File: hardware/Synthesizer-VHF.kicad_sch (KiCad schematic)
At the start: 119 parts, among them J1 Screw_Terminal_01x02, J10 REF_OUT, J11 Header 1x3, J2 Scope, J4 USB-C 2.0 16P, J5 REF_IN, J6 Scope, J7 RFOUTA, J8 Header 1x3, J9 RFOUTB, U1 LM7805A, U11 SN74LVC1GU04DBVR, U2 FT231XQ, U3 ATtiny1616-M, U4 ADF4351, U5 USBLC6-2SC6, U6 LP5907MFX-3.3, U7 ADP150AUJZ-3.3-R7, U8 LP5907MFX-3.3, U9 LP5907MFX-3.3, X1 HCI 8122S-25NQ33FTL

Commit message: diecast-2x2: user layout edits (KiCad save)
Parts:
- removed C44, C45, C46, C47, C48, C49: 100p, Synthesizer:Cap_0402, symbol Device:C
- removed FB2, FB4, FB6: FerriteBead_Small, Inductor_SMD:L_0805_2012Metric, symbol Device:FerriteBead_Small
- removed U7: ADP150AUJZ-3.3-R7, Package_TO_SOT_SMD:SOT-23-5, symbol Synthesizer:ADP150AUJZ-3.3-R7
- added U10: LP5907MFX-3.3, Package_TO_SOT_SMD:SOT-23-5, symbol Regulator_Linear:LP5907MFX-3.3
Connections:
- net 5V: now also U10.1 (IN), U10.3 (EN)
- net GND: now also U10.2 (GND)
- net VCC_1: no longer C13.1, C19.2, C21.2, C27.1, C30.1, U4.28 (DVDD), U4.32 (SDVDD)
- net VDD: no longer C24.1, C25.1, U4.10 (AVDD), U4.6 (Vp)
- net VRF: now also C14.1, U8.5 (OUT)
- net VVCO: now also C39.1, U6.5 (OUT)
- net VADD: now reaches C53.1, U9.5 (OUT)
- net VADD: now also C24.1, C25.1, U4.10 (AVDD), U4.6 (Vp)
- net at D8.2 (A): no longer U3.2 (PA3)
- net REFIN_SEL: no longer names the net of C3.2, R32.2
- new net VDIG: C13.1, C19.2, C21.2, C27.1, C30.1, U10.5 (OUT), U4.28 (DVDD), U4.32 (SDVDD)
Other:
- moved on the sheet: C1, C10, C12, C13, C14, C15, C16, C17, C18, C19, C20, C21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

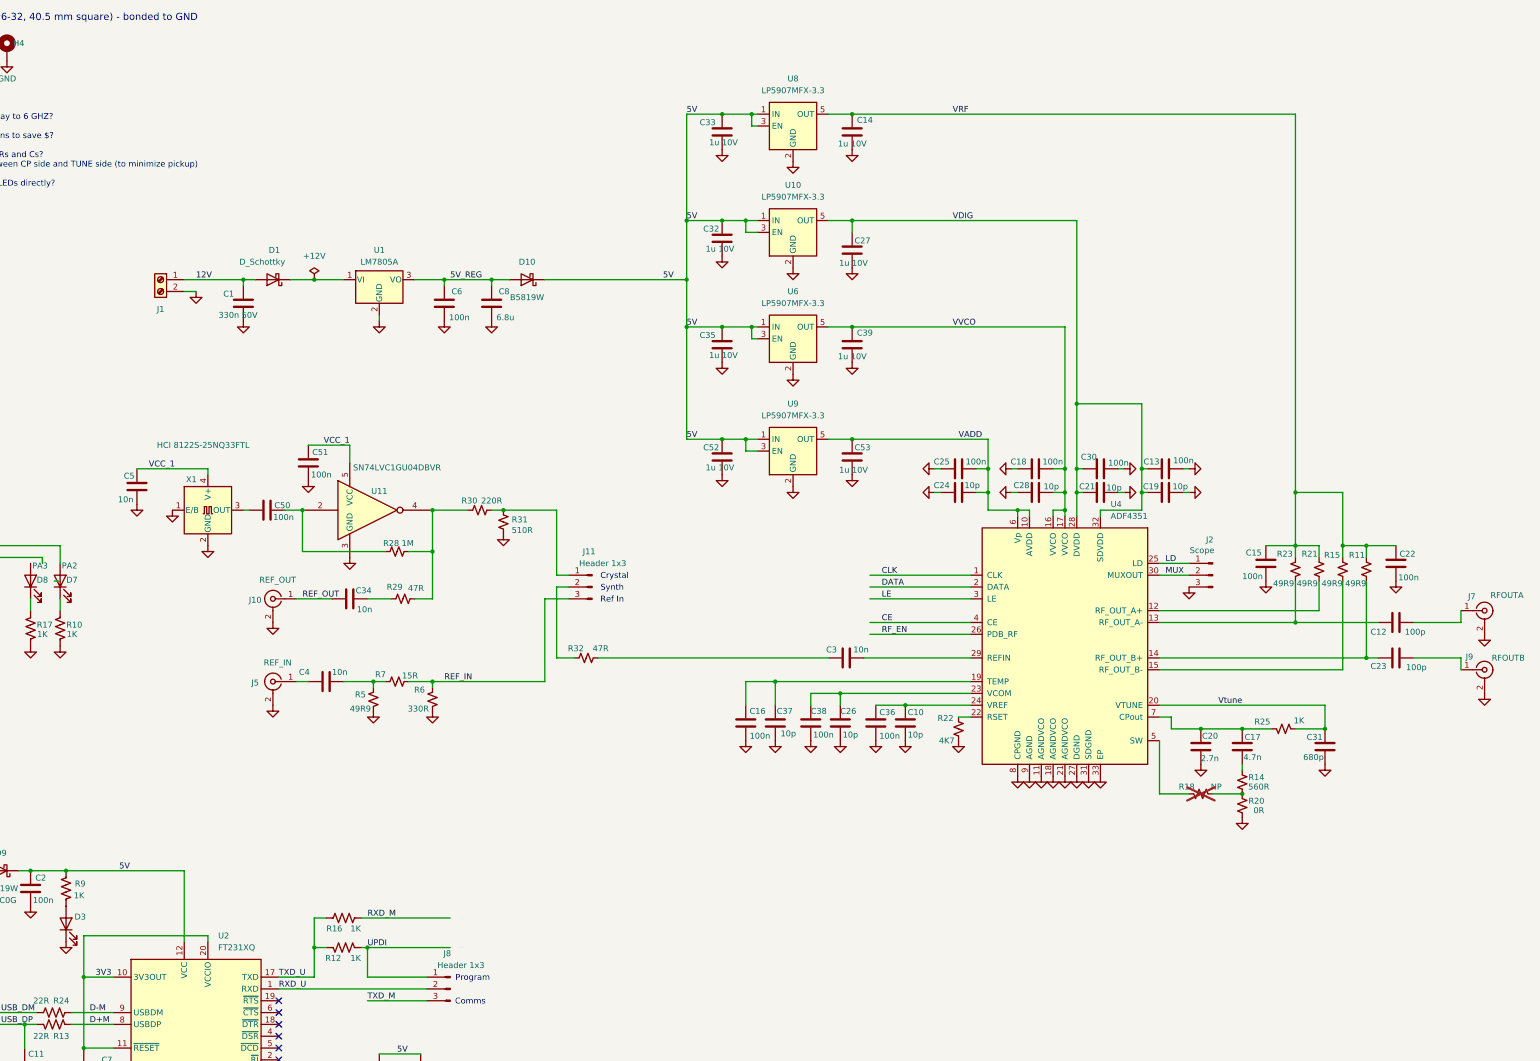
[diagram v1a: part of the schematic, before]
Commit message: diecast-2x2: two LP5907 rails, ferrite-fed 3.3 V digital
Keep U6 for VVCO and U8 for VRF (ADF4351 AVDD/Vp included). Drop U9 and U10. Digital (MCU, FT231X VCCIO, ADF4351 DVDD, ref buffer, VCTCXO) is VDD through FB2 off the VRF LDO. LP5907 LCSC C80670.

Co-authored-by: Jeffrey Millar <wa1hco@users.noreply.github.com>
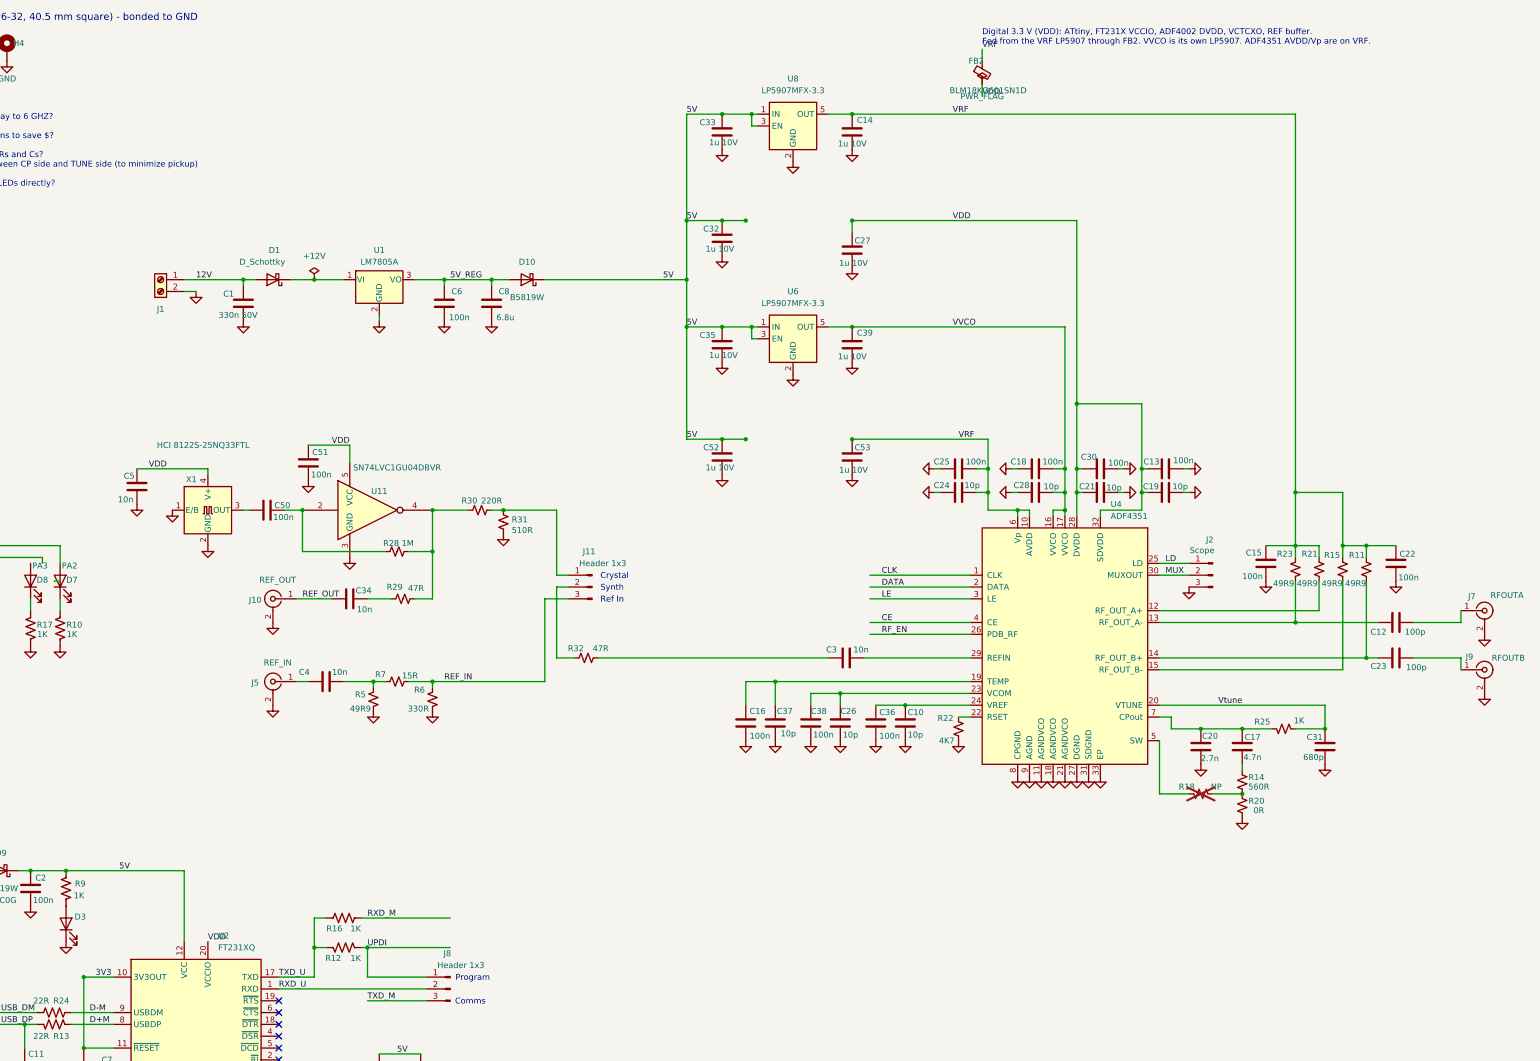
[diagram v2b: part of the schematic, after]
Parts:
- removed U10, U9: LP5907MFX-3.3, Package_TO_SOT_SMD:SOT-23-5, symbol Regulator_Linear:LP5907MFX-3.3
- added FB2: BLM18KG601SN1D, Inductor_SMD:L_0603_1608Metric, symbol Device:FerriteBead_Small
- U6, U8: LCSC (none) -> C80670
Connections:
- net VADD is gone; now on net VRF: C24.1, C25.1, C53.1, U4.10 (AVDD), U4.6 (Vp)
- net VCC_1 is gone; now on net VDD: C5.2, C51.2, U11.5 (VCC), X1.4 (V+)
- net VDIG is gone; now on net VDD: C13.1, C19.2, C21.2, C27.1, C30.1, U4.28 (DVDD), U4.32 (SDVDD)
- net 3V3: no longer U2.20 (VCCIO)
- net VDD: now also U2.20 (VCCIO), FB2.2
- net VRF: now also FB2.1
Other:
- note added: "Digital 3.3 V (VDD): ATtiny, FT231X VCCIO, ADF4002 DVDD, VCTCXO, REF buffer. Fed from the VRF LP5907 through FB2. VVCO is its own LP5907. ADF4351 AVDD/Vp are on VRF."

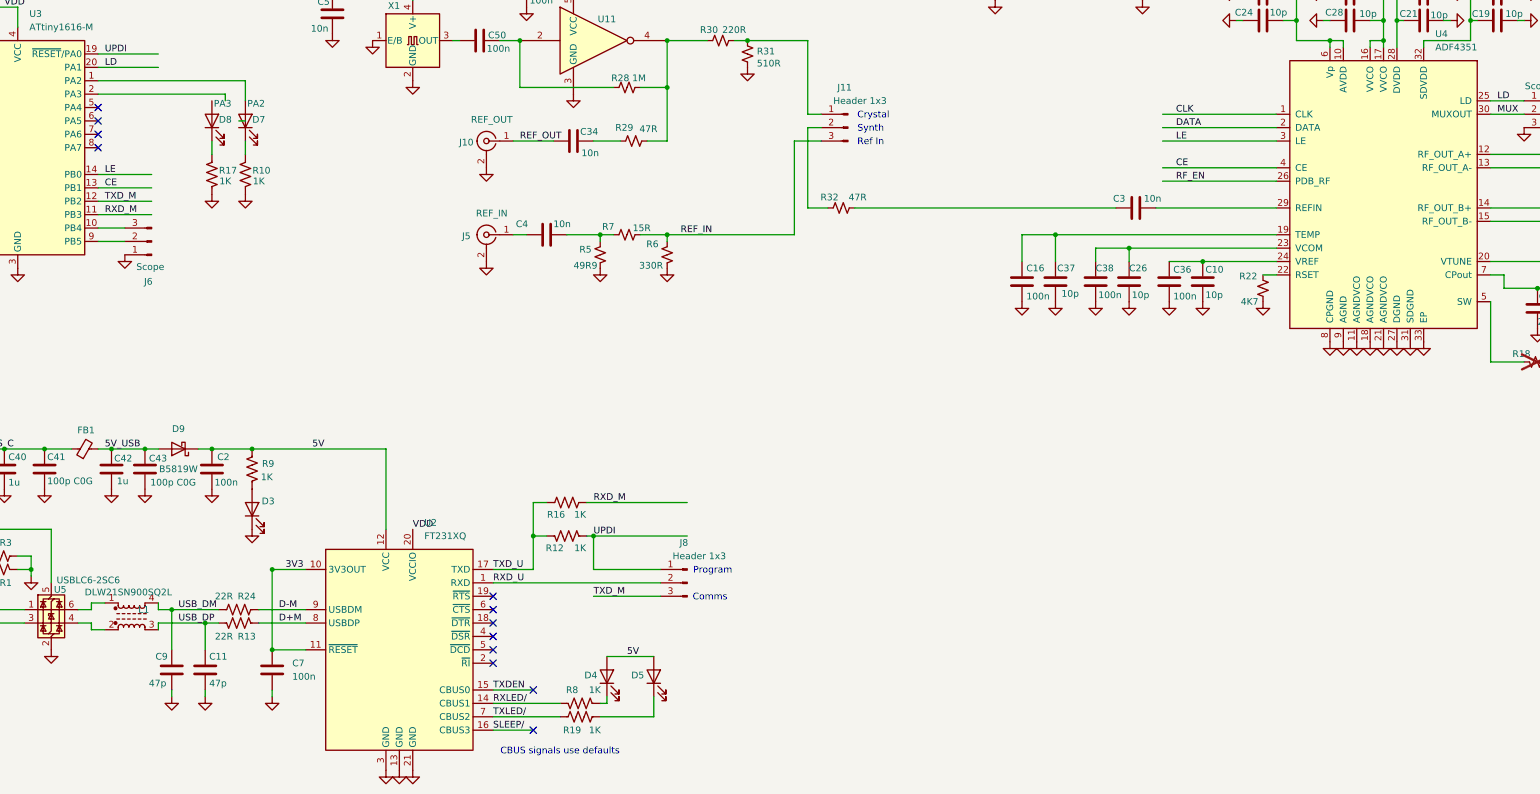
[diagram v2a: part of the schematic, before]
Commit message: diecast-2x2: direct UART, UPDI test pads, Optiboot reset
Remove the J8 program/comm jumper and R12. MCU TX (PB2, TXD_M) drives FT231X RXD; FT231X TXD still drives MCU RX through R16. PA0/UPDI is only on J12 (UPDI, VDD, GND). DTR couples through 100 nF to PA4 with a 10 k pull-up to VDD.

Co-authored-by: Jeffrey Millar <wa1hco@users.noreply.github.com>
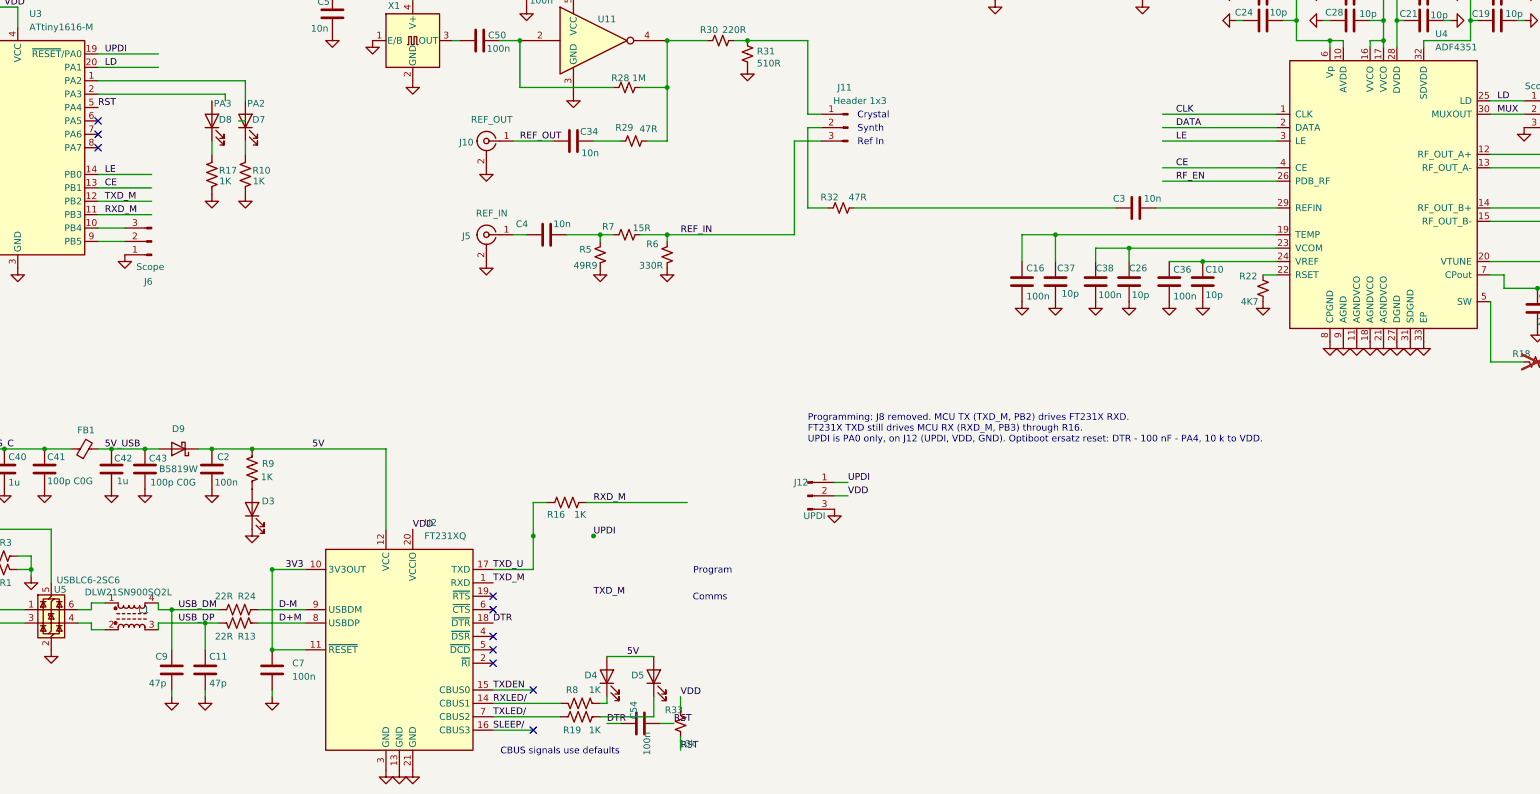
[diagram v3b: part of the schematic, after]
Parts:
- removed J8: Header 1x3, Connector_PinHeader_2.54mm:PinHeader_1x03_P2.54mm_Vertical, symbol Connector:Conn_01x03_Pin
- removed R12: 1K, Synthesizer:Res_0402, symbol Device:R_US
- added C54: 100n, Synthesizer:Cap_0402, symbol Device:C
- added J12: UPDI, Synthesizer:TestPad_1x03_P2.54mm, symbol Connector:Conn_01x03_Pin
- added R33: 10k, Synthesizer:Res_0402, symbol Device:R_Small_US
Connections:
- net RXD_U is gone; now on net TXD_M: U2.1 (RXD)
- net GND: now also J12.3 (Pin_3)
- net UPDI: now also J12.1 (Pin_1)
- net VDD: now also J12.2 (Pin_2), R33.1
- net RST: now reaches U3.5 (PA4)
- net RST: now also C54.2, R33.2
- net DTR: now reaches U2.18 (~{DTR})
- net DTR: now also C54.1
- no-connect marks 14 -> 12
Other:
- note added: "Programming: J8 removed. MCU TX (TXD_M, PB2) drives FT231X RXD. FT231X TXD still drives MCU RX (RXD_M, PB3) through R16. UPDI is PA0 only, on J12 (UPDI, VDD, GND). Optiboot ersatz reset: DTR - 100 nF - PA4, 10 k to VDD."

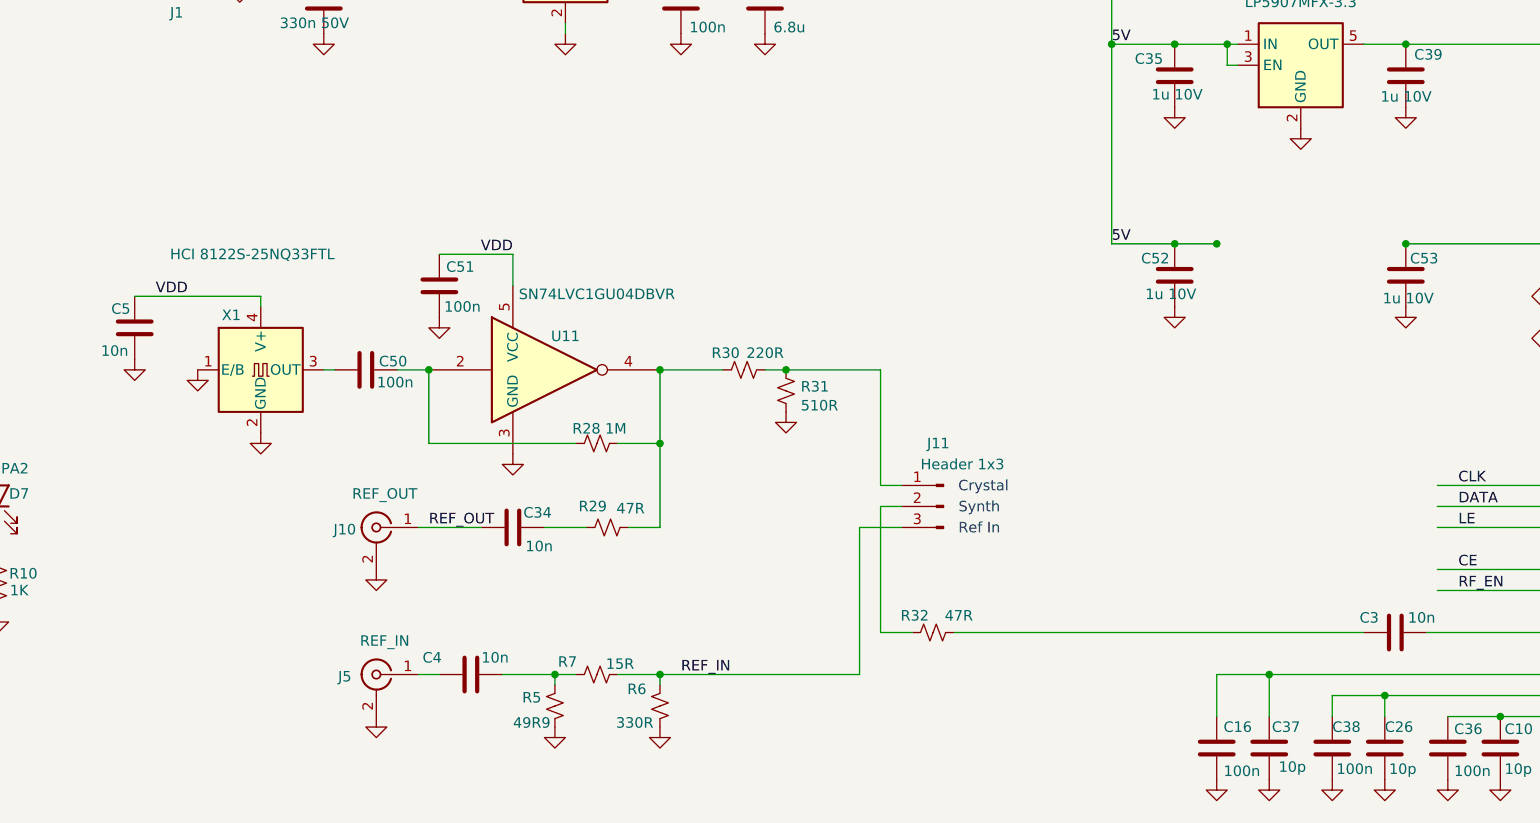
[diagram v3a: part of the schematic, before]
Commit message: diecast-2x2: 10 MHz VCTCXO, drop the ref selector
Replace X1 with a consigned IQD IQXT-220-2 (3225, no LCSC). Its output is AC-coupled to the ADF4351 REFIN and to the REF_OUT buffer. Delete J11 and the selector resistors. REF_OUT after U11 is 39 ohm series plus 100 pF to GND, an edge softener.

Co-authored-by: Jeffrey Millar <wa1hco@users.noreply.github.com>
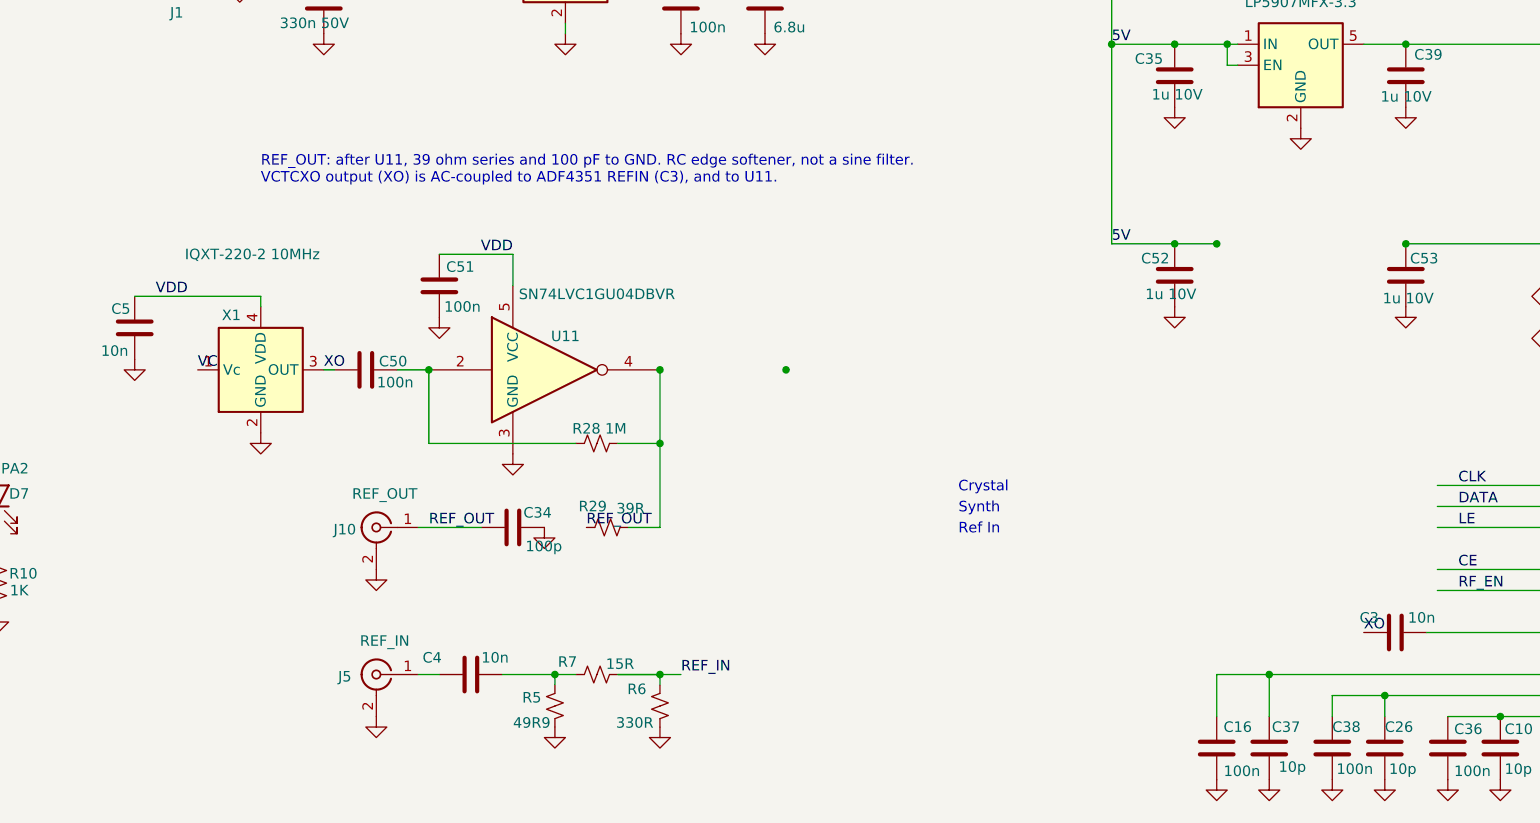
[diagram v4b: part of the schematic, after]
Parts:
- removed J11: Header 1x3, Connector_PinHeader_2.54mm:PinHeader_1x03_P2.54mm_Vertical, symbol Connector:Conn_01x03_Pin
- removed R30: 220R, Synthesizer:Res_0402, symbol Device:R_Small_US
- removed R31: 510R, Synthesizer:Res_0402, symbol Device:R_Small_US
- removed R32: 47R, Synthesizer:Res_0402, symbol Device:R_Small_US
- C34: value 10n -> 100p; LCSC C15195 -> C1546
- R29: value 47R -> 39R; LCSC C25076 -> C185420
- X1: value HCI 8122S-25NQ33FTL -> IQXT-220-2 10MHz; footprint Synthesizer:Oscillator_SMD2520 -> Synthesizer:Oscillator_SMD_3225_VCTCXO; symbol Oscillator:IQXO-70 -> Synthesizer:IQXT-220-2; LCSC C20623084 -> (none)
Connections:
- net GND: now also C34.1; no longer X1.1 (E/B)
- net REF_OUT: now also R29.1
- net XO: now reaches C50.1, X1.3 (OUT)
- net XO: now also C3.2
- new net VC: X1.1 (Vc)
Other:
- note added: "REF_OUT: after U11, 39 ohm series and 100 pF to GND. RC edge softener, not a sine filter. VCTCXO output (XO) is AC-coupled to ADF4351 REFIN (C3), and to U11."
